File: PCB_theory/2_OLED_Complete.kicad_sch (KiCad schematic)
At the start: 2 parts

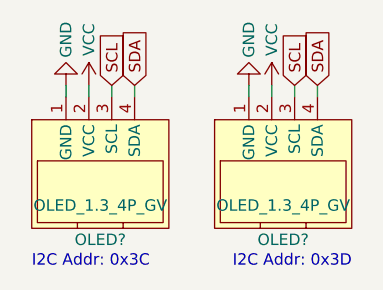
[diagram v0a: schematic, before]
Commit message: fixed annotation in 2_oled
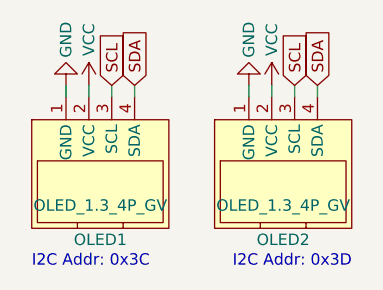
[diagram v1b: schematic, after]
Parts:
- gave numbers to parts that had none: 2
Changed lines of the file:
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@@
   (symbol (lib_id "Custom_Modules:OLED_1.3_4P_GV") (at 30.48 38.1 0) (unit 1)
     (in_bom yes) (on_board yes)
-    (property "Reference" "OLED?" (id 0) (at 30.48 46.355 0))
+    (property "Reference" "OLED1" (id 0) (at 30.48 46.355 0))
     (property "Value" "OLED_1.3_4P_GV" (id 1) (at 30.48 42.545 0))
     (property "Footprint" "Custom_Module:OLED_1.3_4P_M2.5Holes_CleanFront" (id 2) (at 30.48 24.13 0)
@@
   (symbol (lib_id "Custom_Modules:OLED_1.3_4P_GV") (at 50.8 38.1 0) (unit 1)
     (in_bom yes) (on_board yes)
-    (property "Reference" "OLED?" (id 0) (at 50.8 46.355 0))
+    (property "Reference" "OLED2" (id 0) (at 50.8 46.355 0))
     (property "Value" "OLED_1.3_4P_GV" (id 1) (at 50.8 42.545 0))
     (property "Footprint" "Custom_Module:OLED_1.3_4P_M2.5Holes_CleanFront" (id 2) (at 50.8 24.13 0)
